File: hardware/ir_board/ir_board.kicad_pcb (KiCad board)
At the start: 2 copper layers, 30 x 30 mm, 21 parts, among them J1 Conn_01x04, J2 Conn_01x06, Q1 IRLML0030, U1 VL53L0CXV0DH1

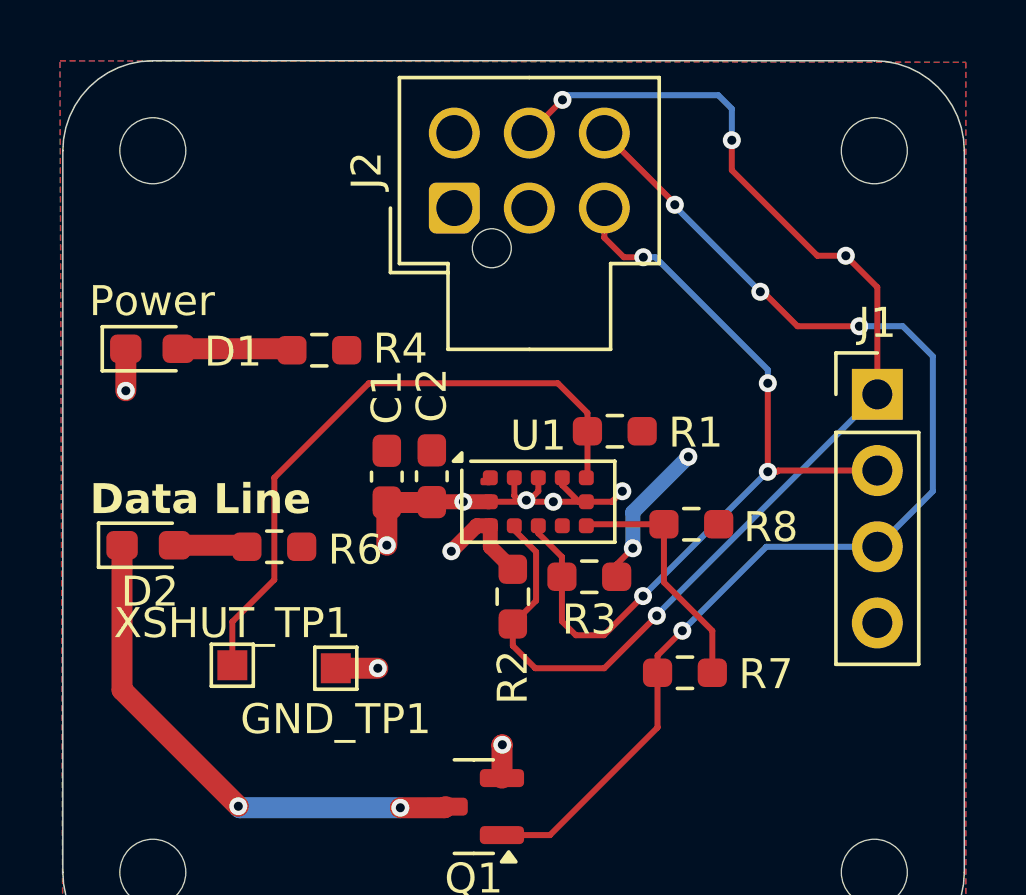
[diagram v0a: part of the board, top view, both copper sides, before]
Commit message: fixed ir-board sensor
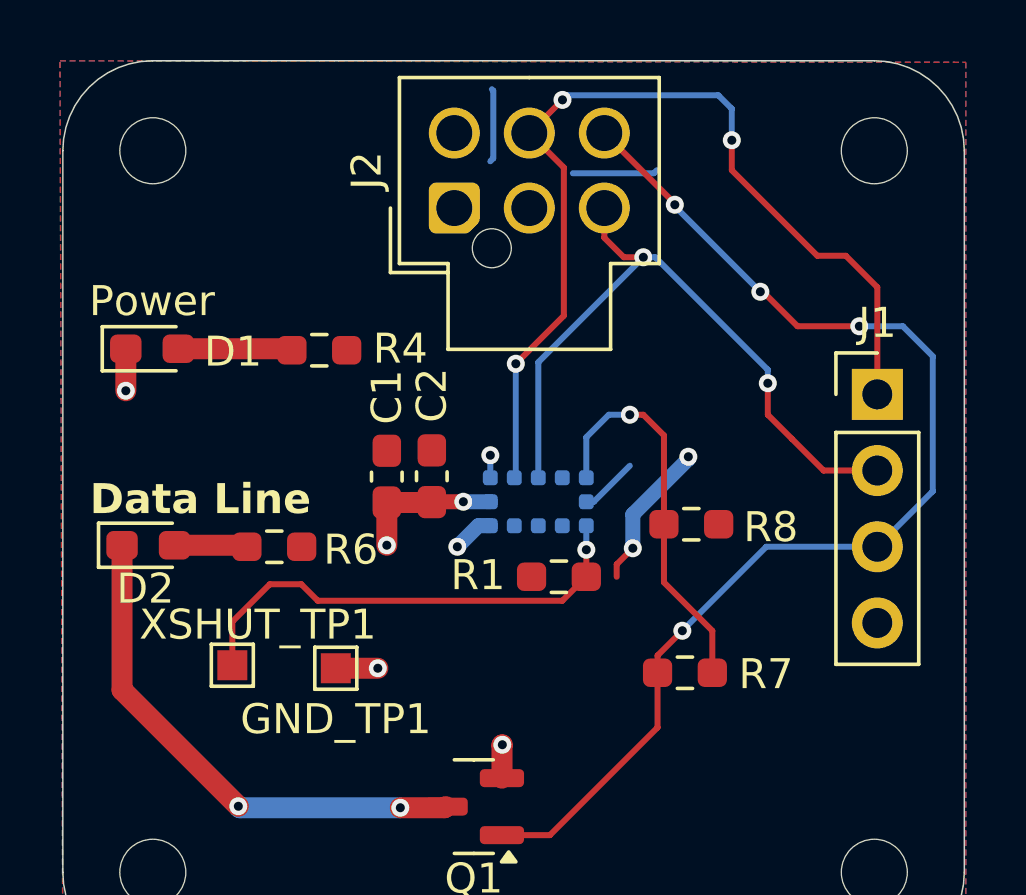
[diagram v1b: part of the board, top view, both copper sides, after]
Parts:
- removed R2, R3: 4.7k, Resistor_SMD:R_0603_1608Metric_Pad0.98x0.95mm_HandSolder
- U1: moved to B.Cu
- moved R1 5.20 mm to (206.6, 52.2), turned to 0 degrees
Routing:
- net /SCL: track 40.4 -> 32.2 mm, vias 4 -> 3
- net /SDA: track 28.2 -> 23.0 mm, vias 4 -> 2
- net /XSHUT: track 21.2 -> 16.0 mm, vias 0 -> 1
- net Net-(U1-GPIO1): track 8.23 -> 13.1 mm, vias 0 -> 1
- net +3.3V: track 8.40 -> 7.13 mm, vias 3 -> 4
- net GND: track 16.7 -> 16.1 mm, vias 8 -> 5

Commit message: finished irboard, tempboard
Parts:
- removed GND_TP1, XSHUT_TP1: TestPoint, TestPoint:TestPoint_Pad_1.0x1.0mm
- added G***: LHRs_LOGO, UTSVT_Logos:LHRs_LOGO, B.Cu at (160.3, 75.9)
- added GND: TestPoint, TestPoint:TestPoint_Pad_1.0x1.0mm, B.Cu at (162.8, 71.5)
- added R2: 4.7k, Resistor_SMD:R_0603_1608Metric_Pad0.98x0.95mm_HandSolder, F.Cu at (162.7, 65.5)
- added R3: 4.7k, Resistor_SMD:R_0603_1608Metric_Pad0.98x0.95mm_HandSolder, F.Cu at (159.4, 65.5)
- added XSHUT: TestPoint, TestPoint:TestPoint_Pad_1.0x1.0mm, B.Cu at (157.1, 71.3)
- D1, D2, J1, J2: moved to B.Cu
- H1, H2, H3, H4: footprint MountingHole:MountingHole_2.2mm_M2 -> MountingHole:MountingHole_3.2mm_M3
- U1: moved to F.Cu
- moved H3 66.8 mm to (151.8, 75.8)
- moved R8 53.2 mm to (164.1, 75.6), turned to -90 degrees
- moved R7 52.6 mm to (162.2, 75.6), turned to 90 degrees
- moved H2 51.1 mm to (169.9, 57.5)
- moved R1 51.0 mm to (159.2, 70.9), turned to 90 degrees
- moved R4 50.9 mm to (152.2, 65.5), turned to -90 degrees
- moved J1 49.7 mm to (170.4, 63.1), turned to 180 degrees
- moved R6 48.8 mm to (152.3, 70.5), turned to 90 degrees
- moved U1 48.6 mm to (160.8, 67.7), turned to 180 degrees
- moved Q1 47.2 mm to (159.2, 75.6)
- moved H1 45.7 mm to (151.7, 57.5)
- moved J2 44.2 mm to (163.3, 59.1)
- moved D1 44.0 mm to (154.8, 66.4), turned to 180 degrees
- moved C2 42.6 mm to (164.2, 67.8), turned to 90 degrees
- moved D2 42.3 mm to (154.8, 69.5), turned to 180 degrees
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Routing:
- net /SDA: track 23.0 -> 35.0 mm, vias 2 -> 0
- net /XSHUT: track 16.0 -> 4.69 mm
- net Net-(D2-K): track 17.3 -> 8.22 mm, vias 2 -> 1
- net +3.3V: track 7.13 -> 15.7 mm, vias 4 -> 8
- net /GPIO1: track 39.1 -> 44.2 mm, vias 4 -> 1
- net Net-(D2-A): track 2.43 -> 4.09 mm, vias 0 -> 1
- net Net-(U1-GPIO1): track 13.1 -> 14.7 mm, vias 1 -> 0
- net GND: track 16.1 -> 17.6 mm, vias 5 -> 4
- net Net-(D1-A): track 3.81 -> 3.45 mm, vias 0 -> 1
- net /SCL: vias 3 -> 0
- added copper zone on B.Cu, net +3.3V
- added copper zone on F.Cu, net GND
- removed copper zone on F.Cu, net +3.3V
- removed copper zone on B.Cu, net GND
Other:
- board size 30 x 30 mm -> 25 x 25 mm
- board text added: "Data"
- board text removed: "Data Line"

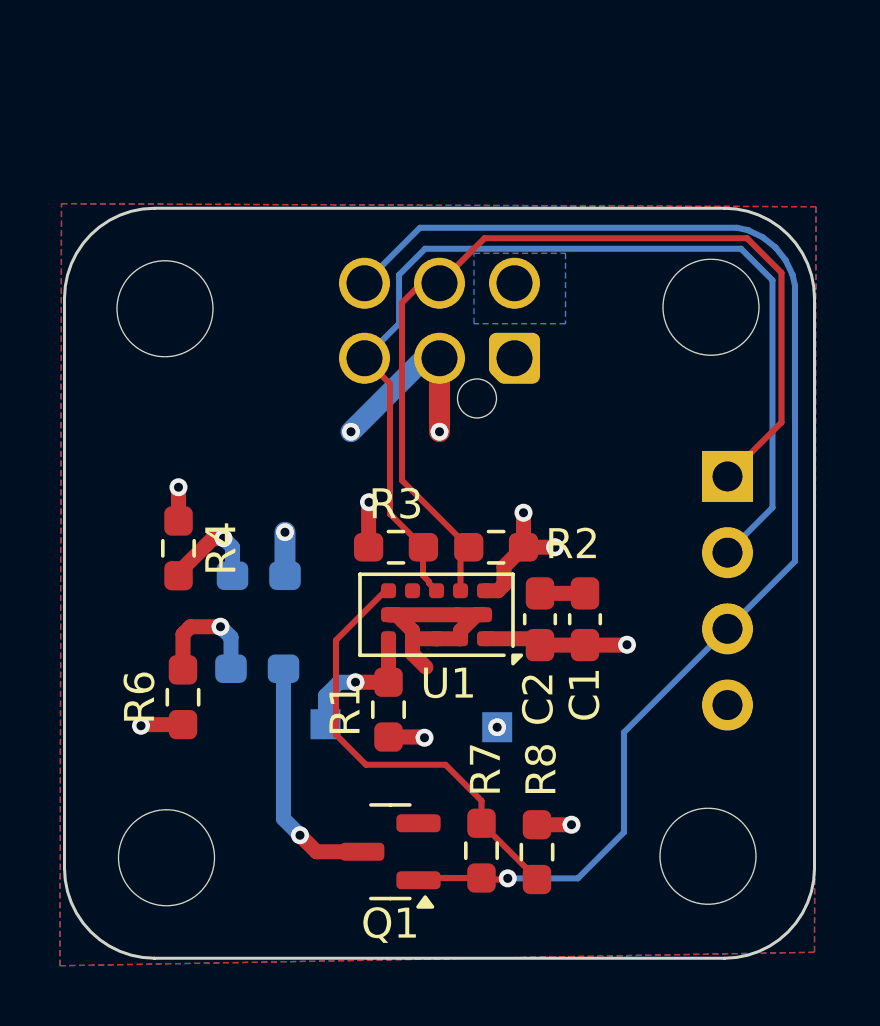
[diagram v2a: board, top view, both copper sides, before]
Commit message: finished ir_board, temp_board with horizontal connectors
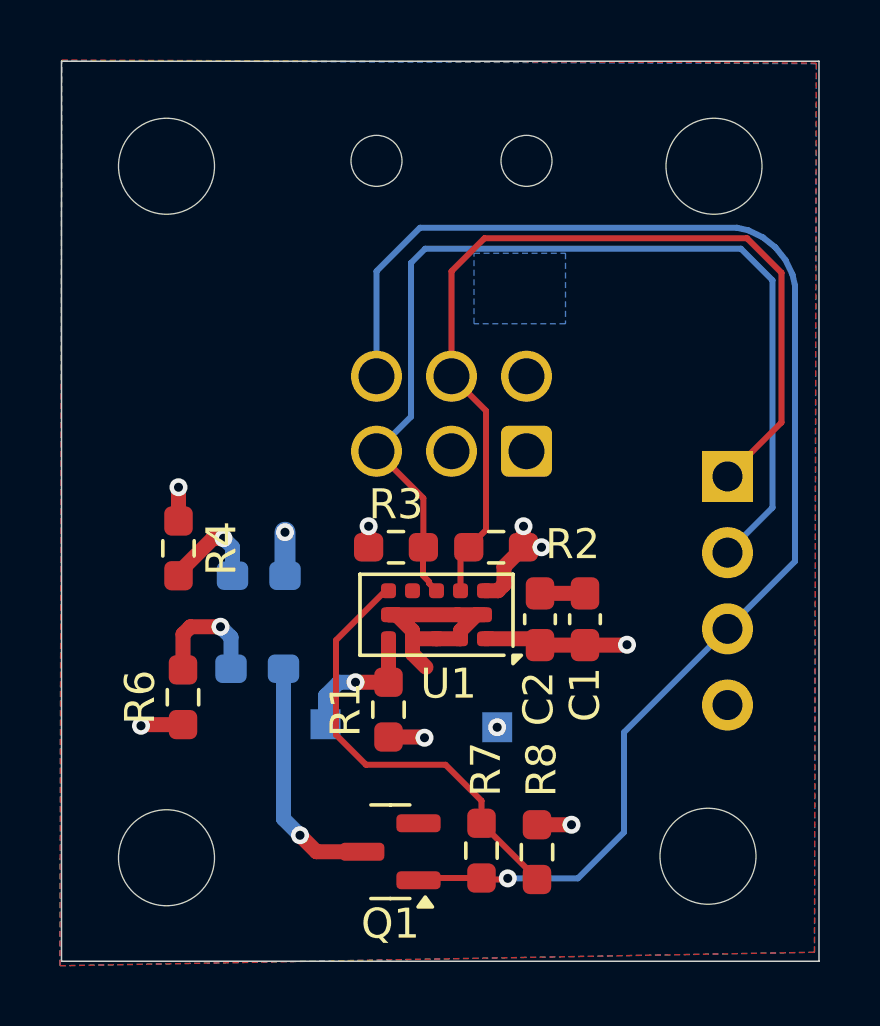
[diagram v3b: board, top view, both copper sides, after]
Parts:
- J2: footprint Connector_Molex:Molex_Nano-Fit_105310-xx06_2x03_P2.50mm_Vertical -> Connector_Molex:Molex_Nano-Fit_105314-xx06_2x03_P2.50mm_Horizontal
- moved H1 4.75 mm to (151.8, 52.8)
- moved H2 4.70 mm to (170.0, 52.8)
- moved J2 3.13 mm to (163.8, 62.2)
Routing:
- net GND: track 17.6 -> 11.2 mm, vias 4 -> 2
- net /GPIO1: track 44.2 -> 48.4 mm
- net +3.3V: track 15.7 -> 14.0 mm
- net /SCL: track 32.2 -> 30.9 mm
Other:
- board size 25 x 25 mm -> 25.2 x 30 mm
